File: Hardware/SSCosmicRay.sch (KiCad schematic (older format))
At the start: 0 parts

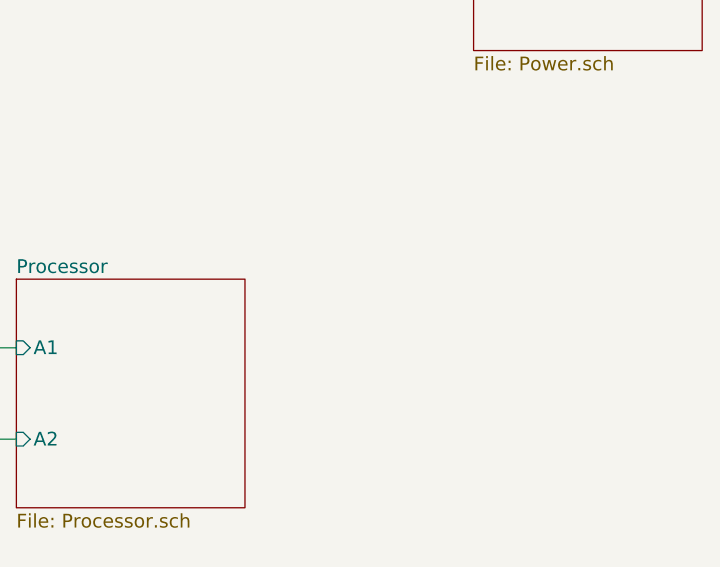
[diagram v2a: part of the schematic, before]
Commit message: Rough layout for pin map testing
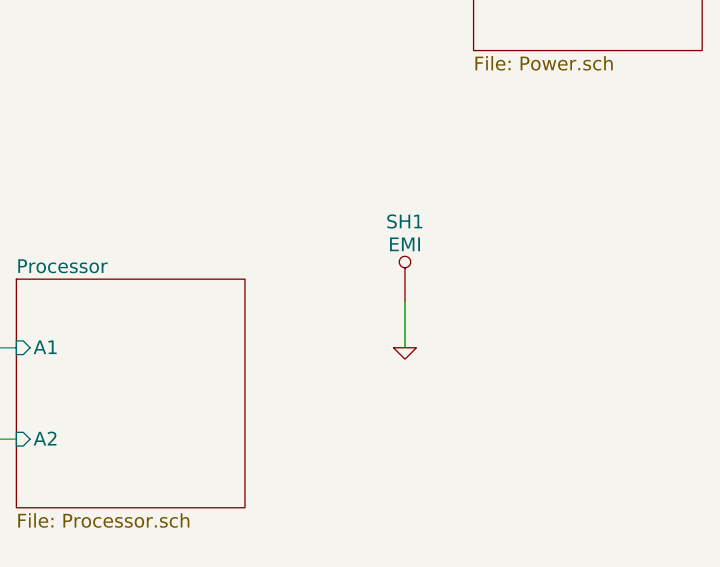
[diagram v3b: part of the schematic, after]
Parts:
- added SH1: EMI, ~, symbol TP
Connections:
- new net GND: SH1.1
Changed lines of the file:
@@
 Sheet 1 5
 Title "Solid State Cosmic Ray Detector"
-Date "25 sep 2014"
+Date "28 sep 2014"
 Rev "1"
 Comp "Ethan Harstad"
@@
 F1 "Power.sch" 60
 $EndSheet
+$Comp
+L TP SH1
+U 1 1 5424BE6A
+P 8100 3500
+F 0 "SH1" H 8100 3850 60  0000 C CNN
+F 1 "EMI" H 8100 3750 60  0000 C CNN
+F 2 "~" H 8100 3500 60  0000 C CNN
+F 3 "~" H 8100 3500 60  0000 C CNN
+	1    8100 3500
+	1    0    0    -1
+$EndComp
+$Comp
+L GND #PWR01
+U 1 1 5424BE85
+P 8100 3700
+F 0 "#PWR01" H 8100 3700 30  0001 C CNN
+F 1 "GND" H 8100 3630 30  0001 C CNN
+F 2 "" H 8100 3700 60  0000 C CNN
+F 3 "" H 8100 3700 60  0000 C CNN
+	1    8100 3700
+	1    0    0    -1
+$EndComp
+Wire Wire Line
+	8100 3700 8100 3500
 $EndSCHEMATC

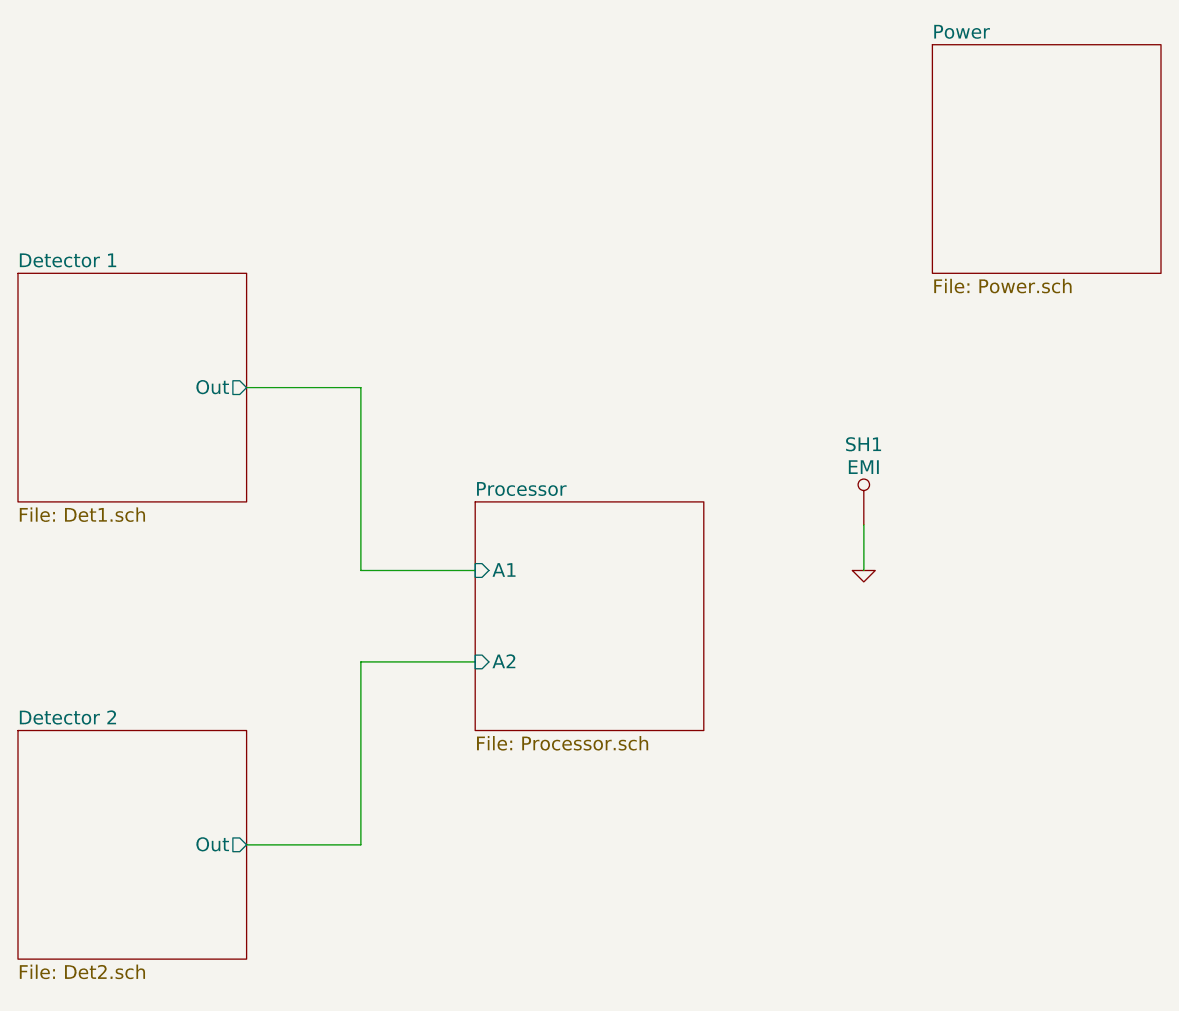
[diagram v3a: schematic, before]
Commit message: Add opamp reference voltage
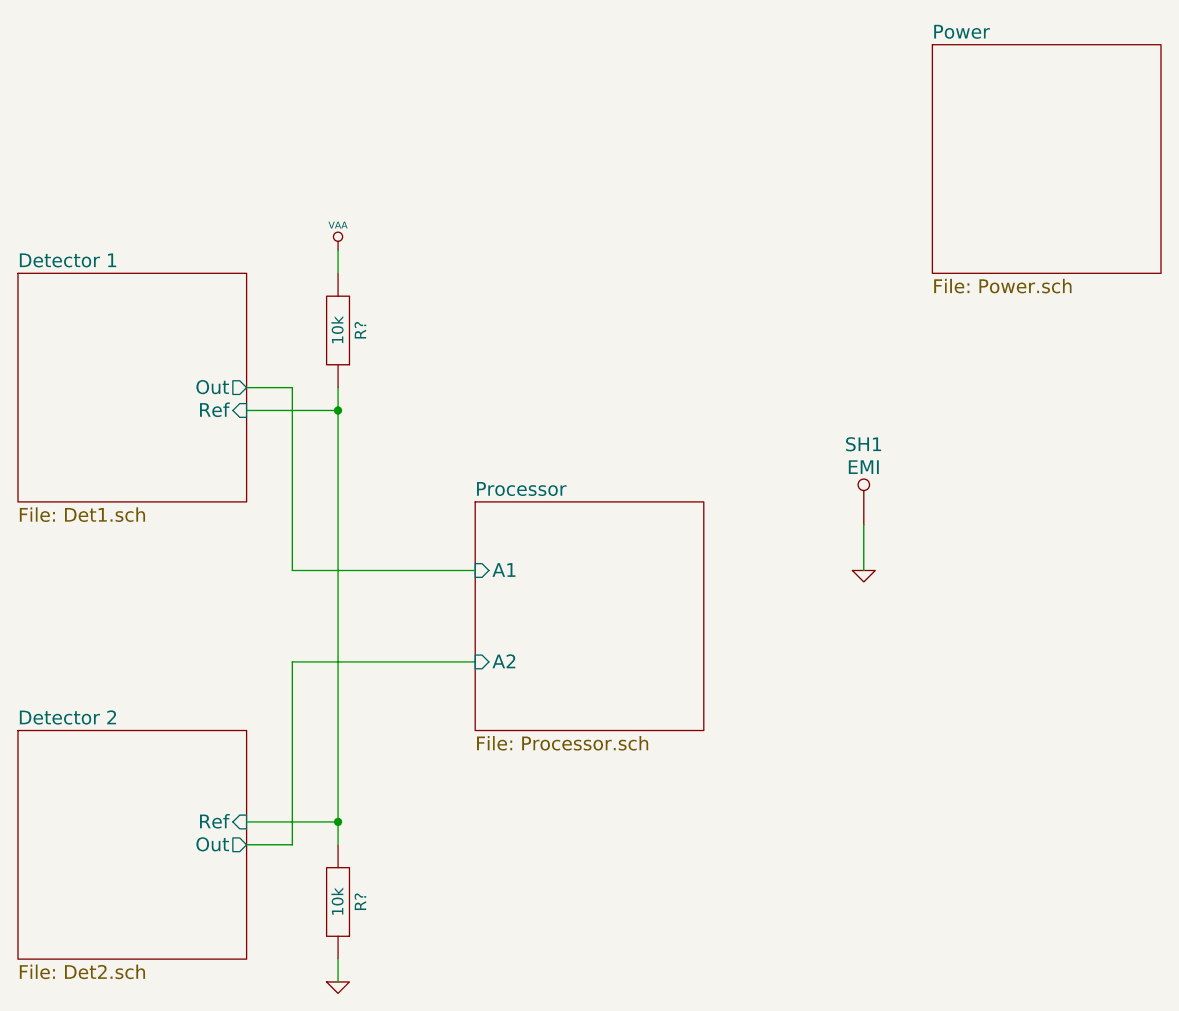
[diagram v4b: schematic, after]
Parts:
- added R? (x2): 10k, RESC1608, symbol R
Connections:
- net GND: now also R?.1
- new net Detector 1/Ref: R?.1, R?.2
- new net VAA: R?.2
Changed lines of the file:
@@
 Sheet 1 5
 Title "Solid State Cosmic Ray Detector"
-Date "28 sep 2014"
+Date "29 sep 2014"
 Rev "1"
 Comp "Ethan Harstad"
@@
 F1 "Det1.sch" 60
 F2 "Out" O R 5400 2900 60
+F3 "Ref" I R 5400 3000 60
 $EndSheet
 Wire Wire Line
-	5400 2900 5900 2900
+	5400 2900 5600 2900
 $Sheet
 S 6400 3400 1000 1000
@@
 $EndSheet
 Wire Wire Line
-	5900 2900 5900 3700
+	5600 2900 5600 3700
 Wire Wire Line
-	5900 3700 6400 3700
+	5600 3700 6400 3700
 $Sheet
 S 4400 4400 1000 1000
@@
 F1 "Det2.sch" 60
 F2 "Out" O R 5400 4900 60
+F3 "Ref" I R 5400 4800 60
 $EndSheet
 Wire Wire Line
-	5400 4900 5900 4900
+	5400 4900 5600 4900
 Wire Wire Line
-	5900 4900 5900 4100
+	5600 4900 5600 4100
 Wire Wire Line
-	5900 4100 6400 4100
+	5600 4100 6400 4100
 $Sheet
 S 8400 1400 1000 1000
@@
 Wire Wire Line
 	8100 3700 8100 3500
+$Comp
+L VAA #PWR?
+U 1 1 5429C8CD
+P 5800 2300
+F 0 "#PWR?" H 5800 2360 30  0001 C CNN
+F 1 "VAA" H 5800 2410 30  0000 C CNN
+F 2 "" H 5800 2300 60  0000 C CNN
+F 3 "" H 5800 2300 60  0000 C CNN
+	1    5800 2300
+	1    0    0    -1
+$EndComp
+$Comp
+L GND #PWR?
+U 1 1 5429C942
+P 5800 5500
+F 0 "#PWR?" H 5800 5500 30  0001 C CNN
+F 1 "GND" H 5800 5430 30  0001 C CNN
+F 2 "" H 5800 5500 60  0000 C CNN
+F 3 "" H 5800 5500 60  0000 C CNN
+	1    5800 5500
+	1    0    0    -1
+$EndComp
+Wire Wire Line
+	5800 5500 5800 5400
+Wire Wire Line
+	5800 2300 5800 2400
+Wire Wire Line
+	5800 2900 5800 4900
+$Comp
+L R R?
+U 1 1 5429CCD3
+P 5800 2650
+F 0 "R?" H 5800 2750 50  0000 C CNN
+F 1 "10k" H 5800 2650 50  0000 C CNN
+F 2 "RESC1608" H 5800 2650 60  0001 C CNN
+F 3 "~" H 5800 2650 60  0000 C CNN
+F 4 "Yageo" H 5800 2650 60  0001 C CNN "MFR Name"
+F 5 "RC0603FR-0710KL" H 5800 2650 60  0001 C CNN "MFR Part No"
+F 6 "311-10.0KHRCT-ND" H 5800 2650 60  0001 C CNN "Distributor Part No"
+F 7 "0.1W" H 5800 2550 50  0001 C CNN "Power"
+F 8 "1%" H 5800 2450 50  0001 C CNN "Tolerance"
+	1    5800 2650
+	0    1    -1   0
+$EndComp
+$Comp
+L R R?
+U 1 1 5429CCFE
+P 5800 5150
+F 0 "R?" H 5800 5250 50  0000 C CNN
+F 1 "10k" H 5800 5150 50  0000 C CNN
+F 2 "RESC1608" H 5800 5150 60  0001 C CNN
+F 3 "~" H 5800 5150 60  0000 C CNN
+F 4 "Yageo" H 5800 5150 60  0001 C CNN "MFR Name"
+F 5 "RC0603FR-0710KL" H 5800 5150 60  0001 C CNN "MFR Part No"
+F 6 "311-10.0KHRCT-ND" H 5800 5150 60  0001 C CNN "Distributor Part No"
+F 7 "0.1W" H 5800 5050 50  0001 C CNN "Power"
+F 8 "1%" H 5800 4950 50  0001 C CNN "Tolerance"
+	1    5800 5150
+	0    1    -1   0
+$EndComp
+Wire Wire Line
+	5400 3000 5800 3000
+Connection ~ 5800 3000
+Wire Wire Line
+	5400 4800 5800 4800
+Connection ~ 5800 4800
 $EndSCHEMATC

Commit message: Change comparator label for better routing
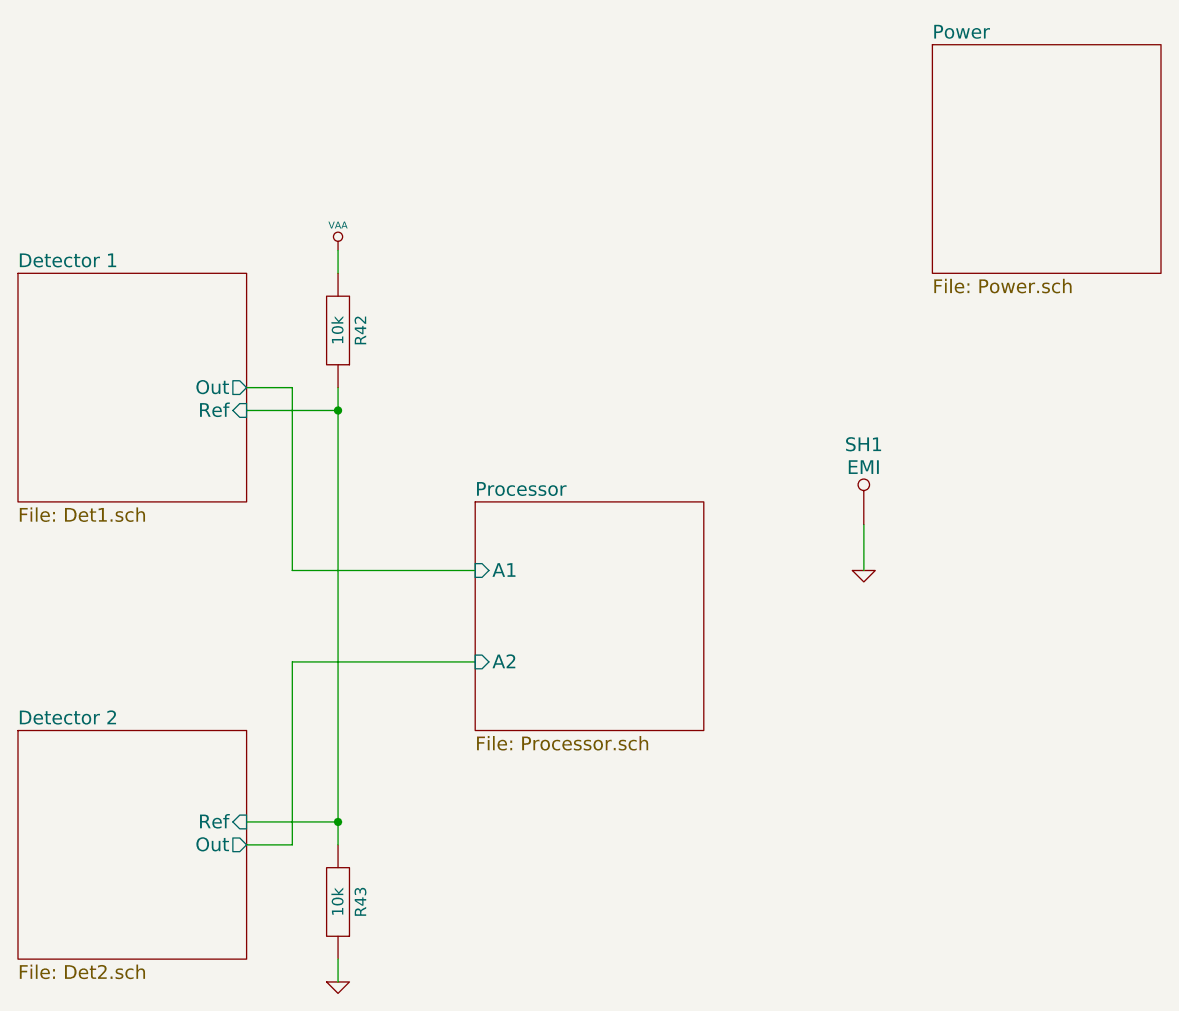
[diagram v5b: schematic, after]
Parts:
- gave numbers to parts that had none: 2
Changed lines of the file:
@@
 	8100 3700 8100 3500
 $Comp
-L VAA #PWR?
+L VAA #PWR02
 U 1 1 5429C8CD
 P 5800 2300
-F 0 "#PWR?" H 5800 2360 30  0001 C CNN
+F 0 "#PWR02" H 5800 2360 30  0001 C CNN
 F 1 "VAA" H 5800 2410 30  0000 C CNN
 F 2 "" H 5800 2300 60  0000 C CNN
@@
 $EndComp
 $Comp
-L GND #PWR?
+L GND #PWR03
 U 1 1 5429C942
 P 5800 5500
-F 0 "#PWR?" H 5800 5500 30  0001 C CNN
+F 0 "#PWR03" H 5800 5500 30  0001 C CNN
 F 1 "GND" H 5800 5430 30  0001 C CNN
 F 2 "" H 5800 5500 60  0000 C CNN
@@
 	5800 2900 5800 4900
 $Comp
-L R R?
+L R R42
 U 1 1 5429CCD3
 P 5800 2650
-F 0 "R?" H 5800 2750 50  0000 C CNN
+F 0 "R42" H 5800 2750 50  0000 C CNN
 F 1 "10k" H 5800 2650 50  0000 C CNN
 F 2 "RESC1608" H 5800 2650 60  0001 C CNN
@@
 $EndComp
 $Comp
-L R R?
+L R R43
 U 1 1 5429CCFE
 P 5800 5150
-F 0 "R?" H 5800 5250 50  0000 C CNN
+F 0 "R43" H 5800 5250 50  0000 C CNN
 F 1 "10k" H 5800 5150 50  0000 C CNN
 F 2 "RESC1608" H 5800 5150 60  0001 C CNN

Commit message: Move interface connector to root sheet
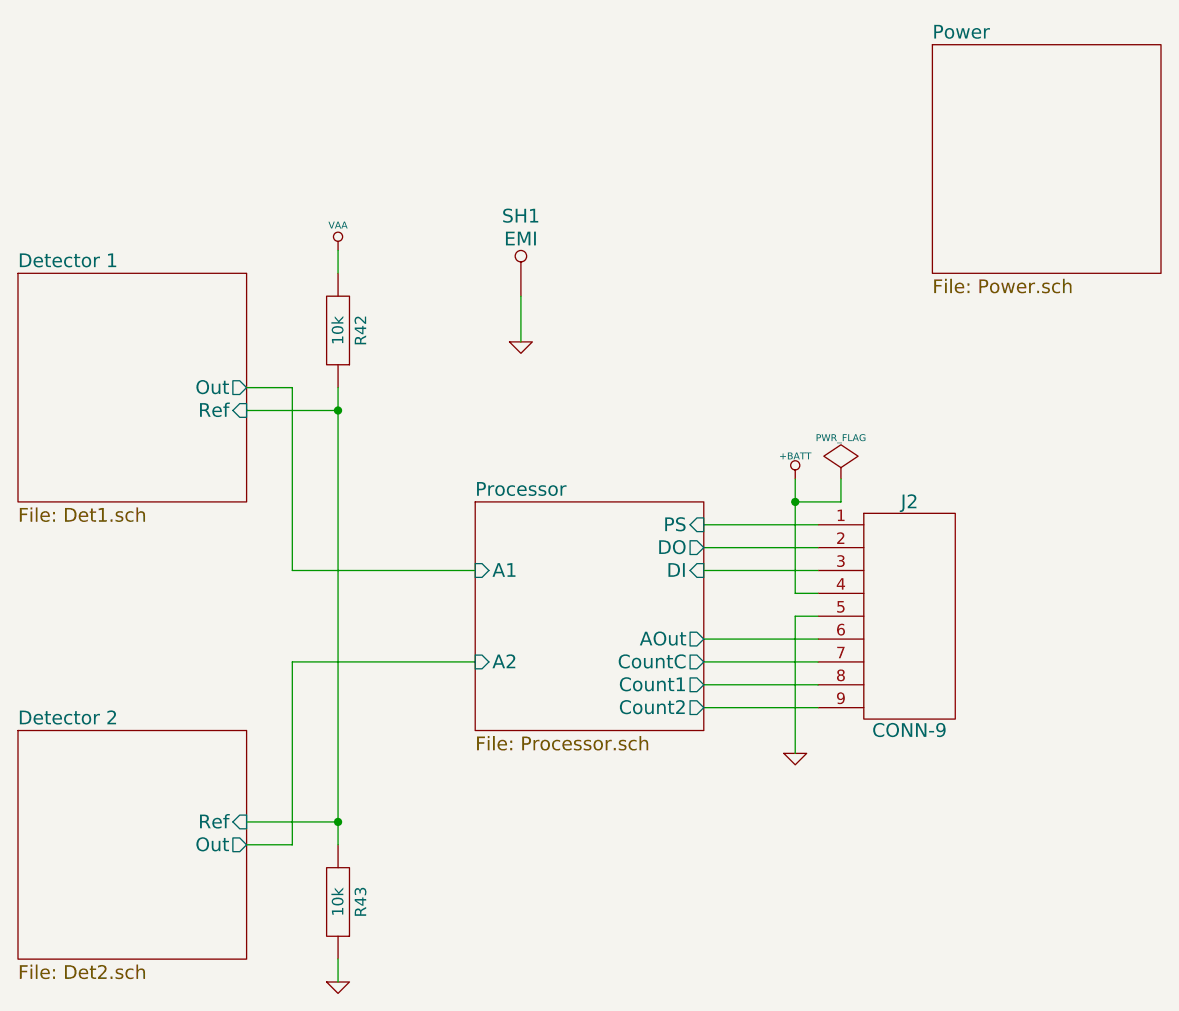
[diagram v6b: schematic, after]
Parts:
- added J2: CONN-9, ~, symbol CONN-9
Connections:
- net GND: now also J2.5
- new net +BATT: J2.4
- new net Processor/AOut: J2.6
- new net Processor/Count1: J2.8
- new net Processor/Count2: J2.9
- new net Processor/CountC: J2.7
- new net Processor/DI: J2.3
- new net Processor/DO: J2.2
- new net Processor/PS: J2.1
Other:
- moved on the sheet: SH1
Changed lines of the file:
@@
 F2 "A1" I L 6400 3700 60
 F3 "A2" I L 6400 4100 60
+F4 "PS" I R 7400 3500 60
+F5 "DO" O R 7400 3600 60
+F6 "DI" I R 7400 3700 60
+F7 "AOut" O R 7400 4000 60
+F8 "CountC" O R 7400 4100 60
+F9 "Count1" O R 7400 4200 60
+F10 "Count2" O R 7400 4300 60
 $EndSheet
 Wire Wire Line
@@
 L TP SH1
 U 1 1 5424BE6A
-P 8100 3500
-F 0 "SH1" H 8100 3850 60  0000 C CNN
-F 1 "EMI" H 8100 3750 60  0000 C CNN
-F 2 "~" H 8100 3500 60  0000 C CNN
-F 3 "~" H 8100 3500 60  0000 C CNN
-	1    8100 3500
+P 6600 2500
+F 0 "SH1" H 6600 2850 60  0000 C CNN
+F 1 "EMI" H 6600 2750 60  0000 C CNN
+F 2 "~" H 6600 2500 60  0000 C CNN
+F 3 "~" H 6600 2500 60  0000 C CNN
+	1    6600 2500
 	1    0    0    -1
 $EndComp
@@
 L GND #PWR01
 U 1 1 5424BE85
-P 8100 3700
-F 0 "#PWR01" H 8100 3700 30  0001 C CNN
-F 1 "GND" H 8100 3630 30  0001 C CNN
-F 2 "" H 8100 3700 60  0000 C CNN
-F 3 "" H 8100 3700 60  0000 C CNN
-	1    8100 3700
+P 6600 2700
+F 0 "#PWR01" H 6600 2700 30  0001 C CNN
+F 1 "GND" H 6600 2630 30  0001 C CNN
+F 2 "" H 6600 2700 60  0000 C CNN
+F 3 "" H 6600 2700 60  0000 C CNN
+	1    6600 2700
 	1    0    0    -1
 $EndComp
 Wire Wire Line
-	8100 3700 8100 3500
+	6600 2700 6600 2500
 $Comp
 L VAA #PWR02
@@
 	5400 4800 5800 4800
 Connection ~ 5800 4800
+$Comp
+L CONN-9 J2
+U 1 1 5429E9E7
+P 8300 3900
+F 0 "J2" H 8300 4400 60  0000 C CNN
+F 1 "CONN-9" H 8300 3400 60  0000 C CNN
+F 2 "~" H 8300 3950 60  0000 C CNN
+F 3 "~" H 8300 3950 60  0000 C CNN
+F 4 "TE" H 8300 3900 60  0001 C CNN "MFR Name"
+F 5 "1734354-2" H 8300 3900 60  0001 C CNN "MFR Part No"
+F 6 "A35108-ND" H 8300 3900 60  0001 C CNN "Distributor Part No"
+	1    8300 3900
+	-1   0    0    -1
+$EndComp
+Wire Wire Line
+	7900 3500 7400 3500
+Wire Wire Line
+	7900 3600 7400 3600
+Wire Wire Line
+	7900 3700 7400 3700
+Wire Wire Line
+	7400 4000 7900 4000
+Wire Wire Line
+	7400 4100 7900 4100
+Wire Wire Line
+	7400 4200 7900 4200
+Wire Wire Line
+	7400 4300 7900 4300
+$Comp
+L +BATT #PWR04
+U 1 1 5429ECBE
+P 7800 3300
+F 0 "#PWR04" H 7800 3250 20  0001 C CNN
+F 1 "+BATT" H 7800 3400 30  0000 C CNN
+F 2 "" H 7800 3300 60  0000 C CNN
+F 3 "" H 7800 3300 60  0000 C CNN
+	1    7800 3300
+	1    0    0    -1
+$EndComp
+$Comp
+L GND #PWR05
+U 1 1 5429ECCD
+P 7800 4500
+F 0 "#PWR05" H 7800 4500 30  0001 C CNN
+F 1 "GND" H 7800 4430 30  0001 C CNN
+F 2 "" H 7800 4500 60  0000 C CNN
+F 3 "" H 7800 4500 60  0000 C CNN
+	1    7800 4500
+	1    0    0    -1
+$EndComp
+$Comp
+L PWR_FLAG #FLG06
+U 1 1 5429ECDC
+P 8000 3300
+F 0 "#FLG06" H 8000 3395 30  0001 C CNN
+F 1 "PWR_FLAG" H 8000 3480 30  0000 C CNN
+F 2 "" H 8000 3300 60  0000 C CNN
+F 3 "" H 8000 3300 60  0000 C CNN
+	1    8000 3300
+	1    0    0    -1
+$EndComp
+Wire Wire Line
+	7800 3300 7800 3800
+Wire Wire Line
+	7800 3800 7900 3800
+Wire Wire Line
+	7900 3900 7800 3900
+Wire Wire Line
+	7800 3900 7800 4500
+Wire Wire Line
+	8000 3300 8000 3400
+Wire Wire Line
+	8000 3400 7800 3400
+Connection ~ 7800 3400
 $EndSCHEMATC
